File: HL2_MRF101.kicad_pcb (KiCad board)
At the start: 4 copper layers, 149.9 x 100 mm, 204 parts, among them J1 Antenna, J2 HL2, J3 RF3, J4 RF1, J5 RCJ-041, J6 50VDC, J7 12V, J8 Fan, J9 HL2_12V, K1 EC2-3NU, K10 EC2-3NU, K11 EC2-3NU, K12 EC2-3NU, K13 EC2-3NU, K2 EC2-3NU, K3 EC2-3NU, K4 EC2-3NU, K5 EC2-3NU, K6 EC2-3NU, K7 EC2-3NU, K8 EC2-3NU, K9 EC2-3NU, Q1 MRF101AN, Q2 2N7002, Q3 NSS60601MZ4, T1 Coupler, T2 Coupler, T3 744851330, U1 MCP6282E/MS, U2 MAX11613, U3 MCP23008, U4 ULN2003, U5 LM35-NEB, U6 MCP4561, U7 INA193

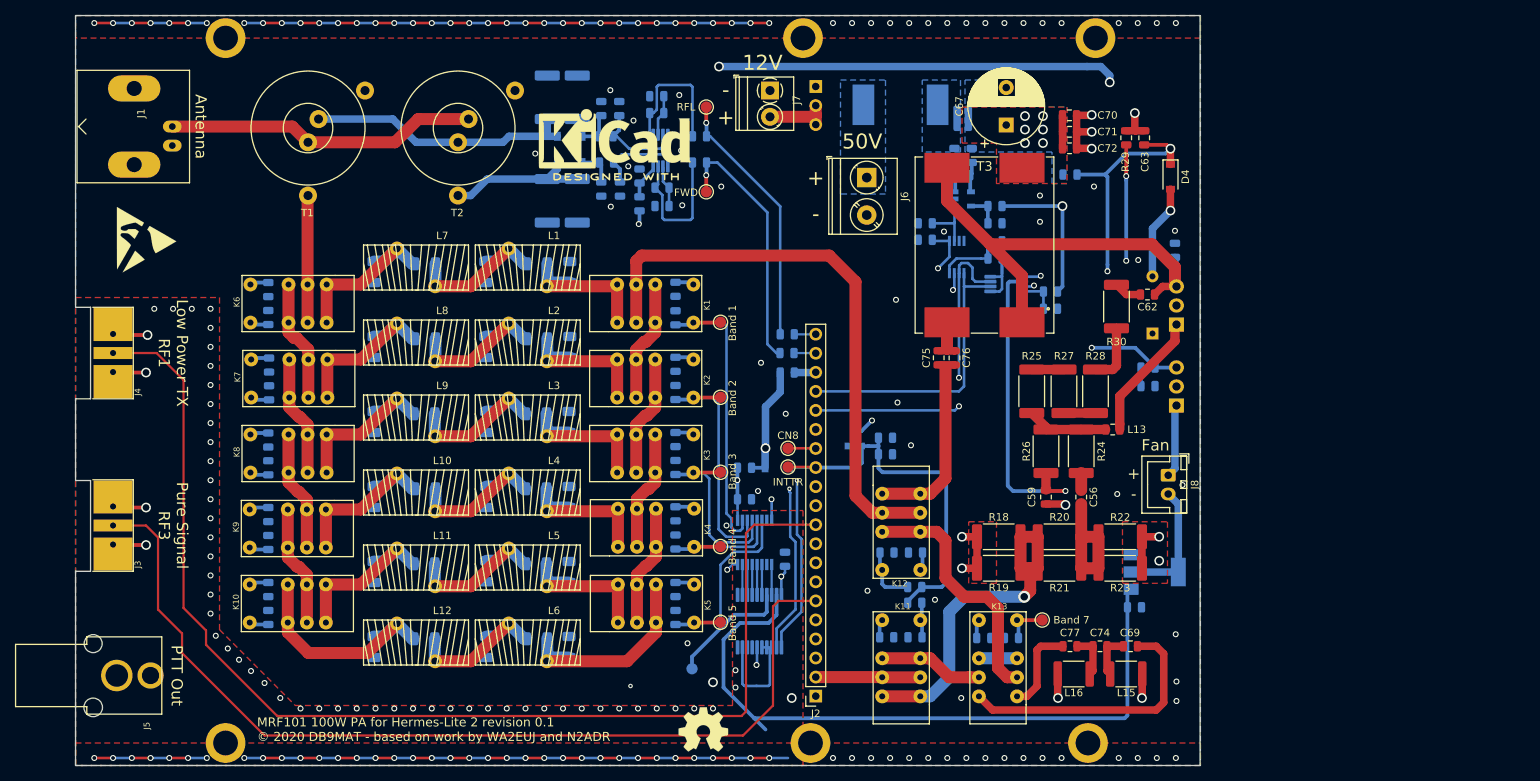
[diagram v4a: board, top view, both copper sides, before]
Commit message: Added ferrites, fan control
Added ferrite beads to relays
Added PWM fan control via DB1 on HL2
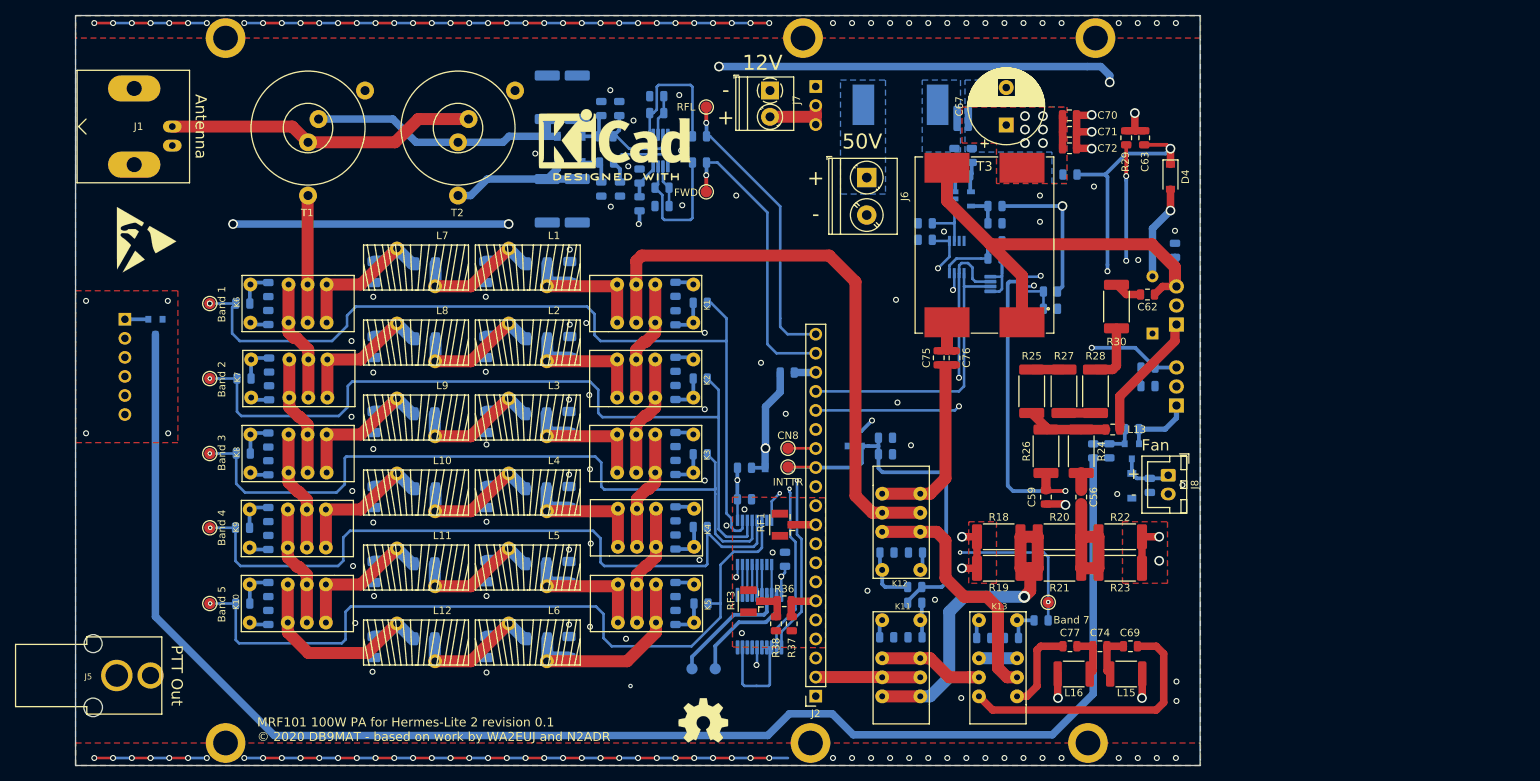
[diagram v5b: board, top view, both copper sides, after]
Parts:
- added C84: 1u, Capacitor_SMD:C_0805_2012Metric, B.Cu at (207.8, 98.0)
- added C85: 1u, Capacitor_SMD:C_0805_2012Metric, B.Cu at (213.2, 102.7)
- added D6: 1N4148W, Diode_SMD:D_SOD-123, B.Cu at (210.8, 102.7)
- added FB10: FB, Inductor_SMD:L_0805_2012Metric, B.Cu at (92.3, 78.4)
- added FB11: FB, Inductor_SMD:L_0805_2012Metric, B.Cu at (153.3, 88.4)
- added FB12: FB, Inductor_SMD:L_0805_2012Metric, B.Cu at (92.5, 88.4)
- added FB13: FB, Inductor_SMD:L_0805_2012Metric, B.Cu at (153.3, 98.5)
- added FB14: FB, Inductor_SMD:L_0805_2012Metric, B.Cu at (92.4, 98.4)
- added FB15: FB, Inductor_SMD:L_0805_2012Metric, B.Cu at (153.3, 108.2)
- added FB16: FB, Inductor_SMD:L_0805_2012Metric, B.Cu at (92.3, 108.3)
- added FB17: FB, Inductor_SMD:L_0805_2012Metric, B.Cu at (153.4, 118.4)
- added FB18: FB, Inductor_SMD:L_0805_2012Metric, B.Cu at (92.3, 118.4)
- added FB19: FB, Inductor_SMD:L_0805_2012Metric, B.Cu at (198.8, 120.7)
- added FB9: FB, Inductor_SMD:L_0805_2012Metric, B.Cu at (153.3, 78.3)
- added J10: DB1, Connector_PinSocket_2.54mm:PinSocket_1x06_P2.54mm_Vertical, B.Cu at (76.6, 80.5)
- added Q4: DTC144E, TO_SOT_Packages_SMD:SOT-23, B.Cu at (80.7, 81.5)
- added R36: TBD, Resistor_SMD:R_0805_2012Metric, F.Cu at (164.5, 118.1)
- added R38: TBD, Resistor_SMD:R_0805_2012Metric, F.Cu at (163.4, 121.1)
- added TP2: P8, TestPoint:TestPoint_Pad_D1.5mm, B.Cu at (155.3, 127.1)
- J3, J4: footprint n2adr:BNCEDGE -> Connector_Coaxial:U.FL_Hirose_U.FL-R-SMT-1_Vertical
- Q3: value NSS60601MZ4 -> IRLML6402; footprint Package_TO_SOT_SMD:SOT-223-3_TabPin2 -> TO_SOT_Packages_SMD:SOT-23
- R16: value 0 -> 10k
- R17: value 0 -> 1k
- R32: value 47k -> 100k
- R37: value 10k -> TBD; moved to F.Cu
- moved J4 94.9 mm to (164.4, 107.9), turned to 180 degrees
- moved J3 88.5 mm to (160.2, 118.1), turned to 180 degrees
- moved TP10 68.1 mm to (87.9, 98.4)
- moved TP11 68.1 mm to (87.9, 108.3)
- moved TP12 68.1 mm to (87.9, 118.4)
- moved TP8 68.1 mm to (87.9, 78.4)
- moved TP9 68.1 mm to (87.9, 88.4)
- moved R16 47.7 mm to (210.8, 95.2)
- moved R37 45.8 mm to (165.5, 121.1), turned to 90 degrees
- moved R17 42.9 mm to (205.7, 98.0), turned to 270 degrees
- moved Q3 16.4 mm to (210.8, 98.1), turned to 270 degrees
- moved TP14 2.48 mm to (199.7, 118.2)
- moved REF** 1.20 mm to (153.7, 134.0) (x2)
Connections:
- C1 pad 2: Band1 -> Net-(C1-Pad2)
- C2 pad 2: Band2 -> Net-(C2-Pad2)
- C3 pad 2: Band3 -> Net-(C3-Pad2)
- C38 pad 2: Band1 -> Net-(C38-Pad2)
- C39 pad 2: Band2 -> Net-(C39-Pad2)
- C4 pad 2: Band4 -> Net-(C4-Pad2)
- C40 pad 2: Band3 -> Net-(C40-Pad2)
- C41 pad 2: Band4 -> Net-(C41-Pad2)
- C42 pad 2: Band5 -> Net-(C42-Pad2)
- C5 pad 2: Band5 -> Net-(C5-Pad2)
- C64 pad 2: Band7 -> Net-(C64-Pad2)
- J2 pad 19: Net-(J2-Pad19) -> FWD_DET
- J2 pad 20: Net-(J2-Pad20) -> RFL_DET
- J3 pad 1: Net-(J2-Pad6) -> Net-(J3-Pad1)
- J8 pad 1: +12V -> Net-(C85-Pad2)
- J8 pad 2: Net-(J8-Pad2) -> GND
- K1 pad 8: Band1 -> Net-(C1-Pad2)
- K10 pad 8: Band5 -> Net-(C42-Pad2)
- K13 pad 8: Band7 -> Net-(C64-Pad2)
- K2 pad 8: Band2 -> Net-(C2-Pad2)
- K3 pad 8: Band3 -> Net-(C3-Pad2)
- K4 pad 8: Band4 -> Net-(C4-Pad2)
- K5 pad 8: Band5 -> Net-(C5-Pad2)
- K6 pad 8: Band1 -> Net-(C38-Pad2)
- K7 pad 8: Band2 -> Net-(C39-Pad2)
- K8 pad 8: Band3 -> Net-(C40-Pad2)
- K9 pad 8: Band4 -> Net-(C41-Pad2)
- Q3 pad 1: Fan_Ctrl -> Net-(C84-Pad2)
- Q3 pad 2: Net-(J8-Pad2) -> +12V
- Q3 pad 3: GND -> Net-(C85-Pad2)
- R16 pad 1: Net-(J2-Pad20) -> +12V
- R16 pad 2: RFL_DET -> Net-(C84-Pad2)
- R17 pad 1: Net-(J2-Pad19) -> Net-(C84-Pad2)
- R17 pad 2: FWD_DET -> Net-(Q4-Pad3)
- R37 pad 2: Fan_Ctrl -> Net-(J2-Pad6)
- U3 pad 19: Fan_Ctrl -> Net-(TP2-Pad1)
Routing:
- net Net-(Q4-Pad3): track 0.00 -> 205.3 mm
- net Net-(J2-Pad10): track 157.2 -> 3.25 mm
- net Net-(J2-Pad6): track 127.6 -> 5.37 mm
- net Fan_Ctrl: track 92.4 -> 0.00 mm
- net +3V3: track 497.3 -> 535.5 mm, vias 10 -> 9
- net GND: track 261.7 -> 243.8 mm, vias 205 -> 188
- net Net-(J8-Pad2): track 17.3 -> 0.00 mm
- net Net-(TP2-Pad1): track 0.00 -> 15.3 mm
- net Band4: track 82.2 -> 95.0 mm, vias 0 -> 1
- net Band3: track 88.5 -> 98.6 mm, vias 0 -> 1
- net Band5: track 91.8 -> 101.8 mm, vias 0 -> 1
- net Band2: track 97.3 -> 107.0 mm, vias 0 -> 1
- net Band1: track 105.2 -> 114.7 mm, vias 0 -> 1
- net EXTTR: track 137.0 -> 127.6 mm
- net Net-(C85-Pad2): track 0.00 -> 7.25 mm
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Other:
- outline, holes or cut-outs redrawn
- board text removed: "Low Power TX Out"
- board text removed: "Low Power TX RF1"
- board text removed: "Pure Signal RF3"
- board text removed: "Pure Signal Sample"

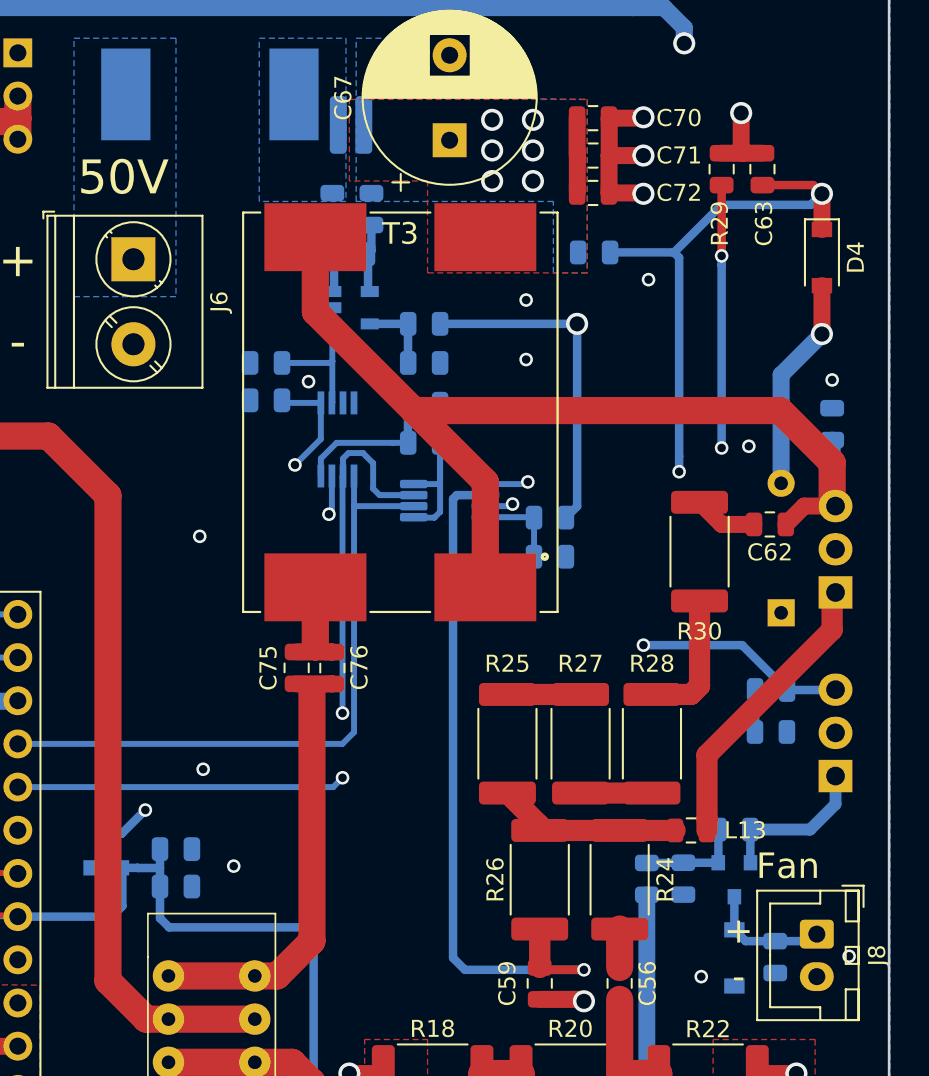
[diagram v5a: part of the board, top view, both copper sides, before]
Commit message: Reworked bias circuit
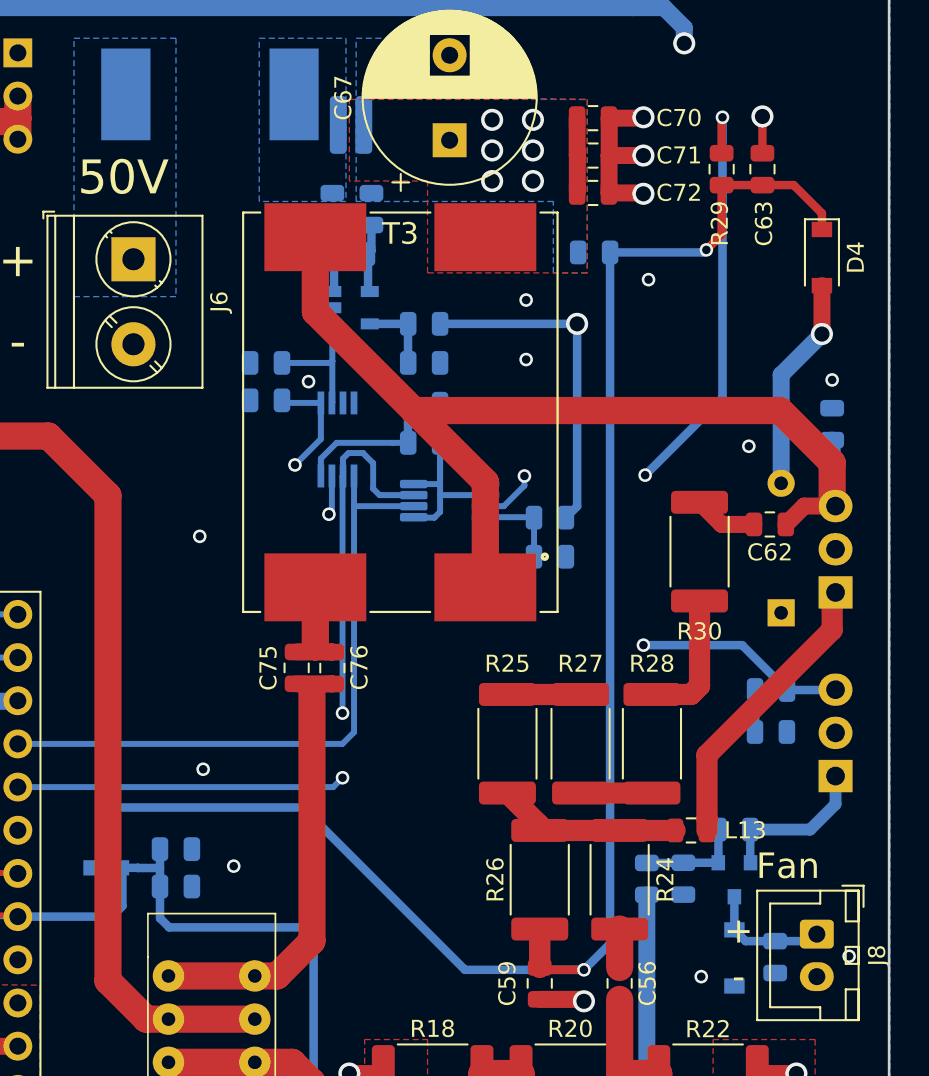
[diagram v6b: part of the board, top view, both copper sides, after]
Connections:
- C63 pad 2: Net-(C63-Pad2) -> Net-(C59-Pad1)
- D4 pad 1: Net-(C63-Pad2) -> Net-(C59-Pad1)
- Q2 pad 3: Net-(C63-Pad2) -> Net-(C59-Pad1)
- R29 pad 1: Net-(R29-Pad1) -> Net-(C59-Pad1)
- R29 pad 2: GND -> Net-(R29-Pad2)
- R32 pad 2: Net-(C63-Pad2) -> Net-(C59-Pad1)
- U6 pad 5: Net-(C63-Pad2) -> Net-(U6-Pad5)
- U6 pad 6: Net-(C59-Pad1) -> GND
- U6 pad 7: Net-(R29-Pad1) -> Net-(R29-Pad2)
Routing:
- net Net-(C63-Pad2): track 97.9 -> 0.00 mm, vias 4 -> 0
- net Net-(C59-Pad1): track 41.9 -> 98.5 mm, vias 1 -> 2
- net Net-(R29-Pad2): track 0.00 -> 35.5 mm, vias 0 -> 3
- net Net-(R29-Pad1): track 32.1 -> 0.00 mm, vias 3 -> 0

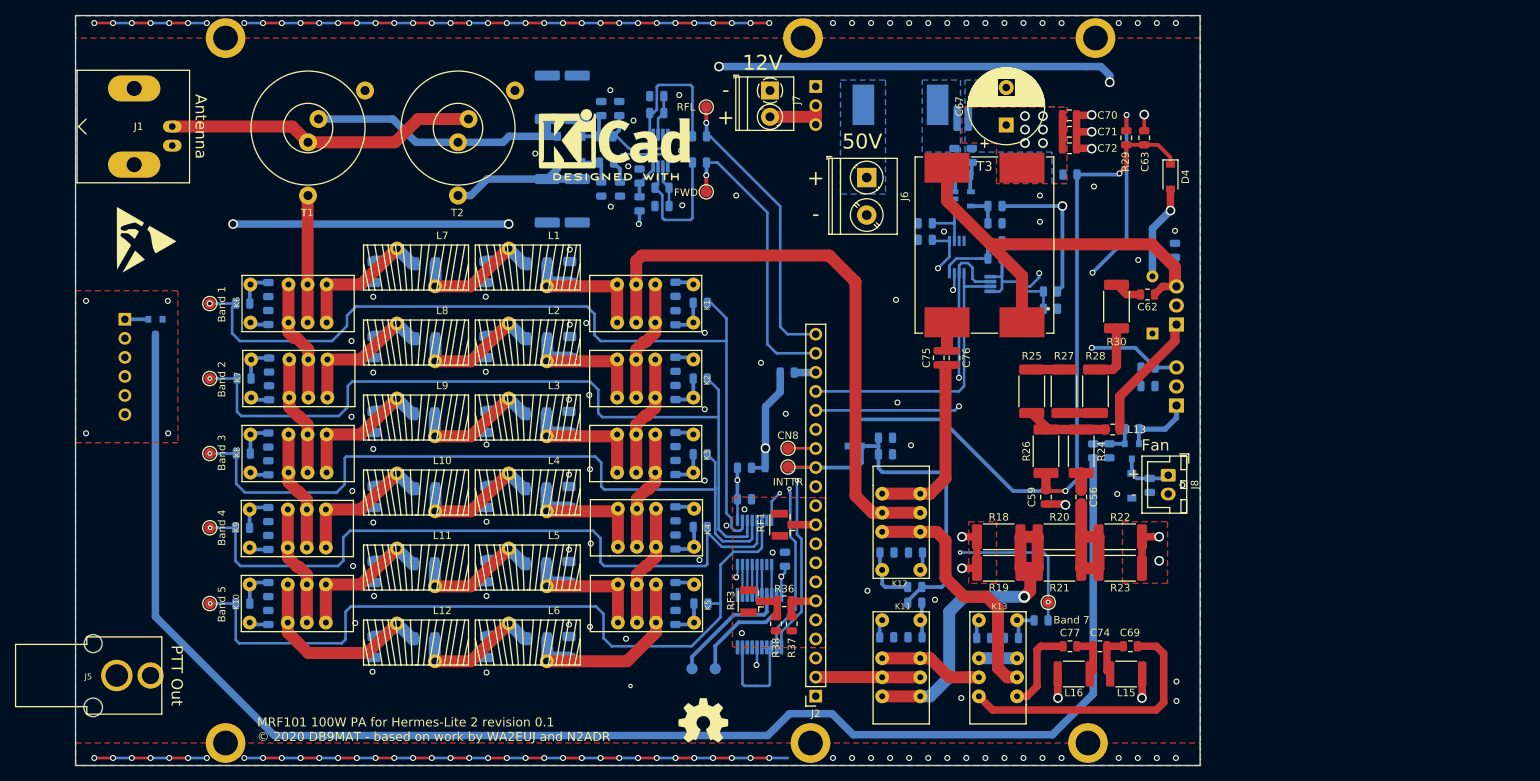
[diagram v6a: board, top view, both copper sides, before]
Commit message: Reworked bias circuit, again.
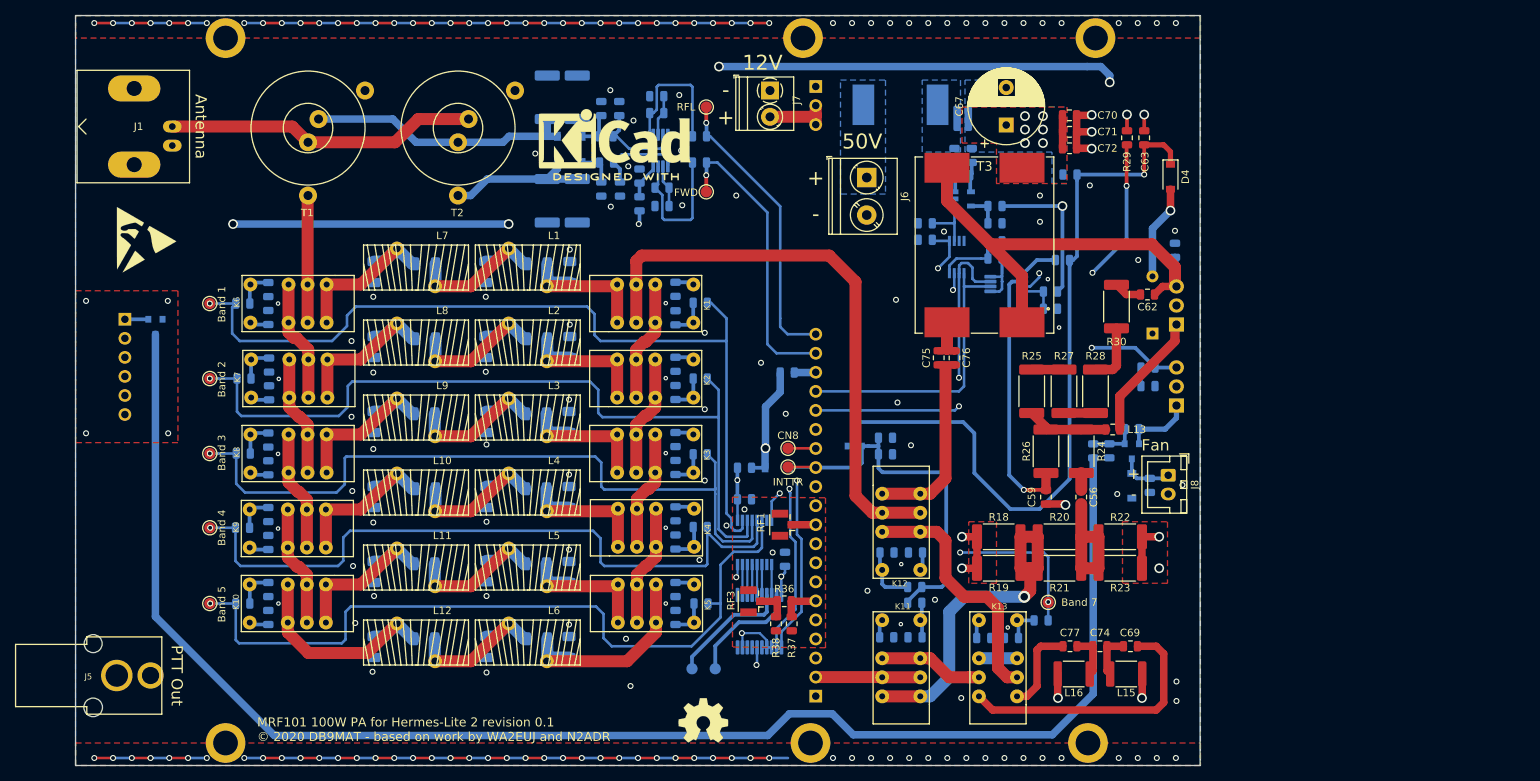
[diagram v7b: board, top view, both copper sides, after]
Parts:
- added R39: 5k6, Resistor_SMD:R_0805_2012Metric, B.Cu at (201.6, 72.6)
- J2: moved to B.Cu
- R32: value 100k -> 47k
- moved R29 0.10 mm to (210.2, 56.3), turned to 270 degrees
- turned J2 to 0 degrees
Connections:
- C63 pad 2: Net-(C59-Pad1) -> Net-(C63-Pad2)
- D4 pad 1: Net-(C59-Pad1) -> Net-(C63-Pad2)
- Q2 pad 3: Net-(C59-Pad1) -> Net-(C63-Pad2)
- R29 pad 1: Net-(C59-Pad1) -> GND
- R32 pad 2: Net-(C59-Pad1) -> Net-(C63-Pad2)
- U6 pad 6: GND -> Net-(C59-Pad1)
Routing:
- net Net-(C63-Pad2): track 0.00 -> 99.1 mm, vias 0 -> 1
- net Net-(C59-Pad1): track 98.5 -> 35.3 mm, vias 2 -> 1
- net GND: track 243.8 -> 236.2 mm, vias 188 -> 199
- net Net-(R29-Pad2): track 35.5 -> 29.4 mm
- net Net-(R39-Pad2): track 0.00 -> 5.52 mm

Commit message: Impedance Adjustment started
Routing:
- net +12V: track 117.4 -> 18.0 mm
- net Vtemp: track 48.0 -> 68.6 mm, vias 2 -> 4
- net Net-(R29-Pad2): track 29.4 -> 21.8 mm, vias 3 -> 1
- net Net-(C62-Pad1): track 60.2 -> 63.0 mm
- net +3V3: track 535.5 -> 536.7 mm
- net GND: vias 199 -> 204
